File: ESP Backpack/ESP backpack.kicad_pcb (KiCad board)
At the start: 2 copper layers, 100 x 100 mm, 33 parts, among them J1 HLE-120-02-F-DV-BE-K, J2 HLE-120-02-F-DV-BE-K, U1 ESP32-DEVKITC-32D, U2 VCNL4010-GS08

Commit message: edit weird fill issue
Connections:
- J1 pad 30: Net-(J1-Pad30) -> GND
- J1 pad 34: Net-(J1-Pad34) -> GND
- J1 pad 38: Net-(J1-Pad38) -> GND
- J2 pad 29: Net-(J2-Pad29) -> +5V
- J2 pad 30: Net-(J2-Pad30) -> GND
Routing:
- net Net-(J1-Pad34): track 1.41 -> 0.00 mm
- net GND: track 28.5 -> 29.9 mm

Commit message: reorg to more standard file tree
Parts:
- D1: footprint LED_SK6812 -> _ESP-Backpack-Custom-Libraries:LED_SK6812
- J1, J2: footprint Custom Libraries:SAMTEC_HLE-120-02-F-DV-BE-K -> _ESP-Backpack-Custom-Libraries:SAMTEC_HLE-120-02-F-DV-BE-K
- S1, S2: footprint 452403012014 -> _ESP-Backpack-Custom-Libraries:452403012014
- U1: footprint Custom Libraries:MODULE_ESP32-DEVKITC-32D -> _ESP-Backpack-Custom-Libraries:MODULE_ESP32-DEVKITC-32D
- U2: footprint Custom Libraries:XDCR_VCNL4010-GS08 -> _ESP-Backpack-Custom-Libraries:XDCR_VCNL4010-GS08
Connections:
- J1 pad 30: GND -> Net-(J1-Pad30)
- J1 pad 34: GND -> Net-(J1-Pad34)
- J1 pad 38: GND -> Net-(J1-Pad38)
- J2 pad 29: +5V -> Net-(J2-Pad29)
- J2 pad 30: GND -> Net-(J2-Pad30)
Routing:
- net Net-(J1-Pad34): track 0.00 -> 1.41 mm
- net GND: track 29.9 -> 28.5 mm

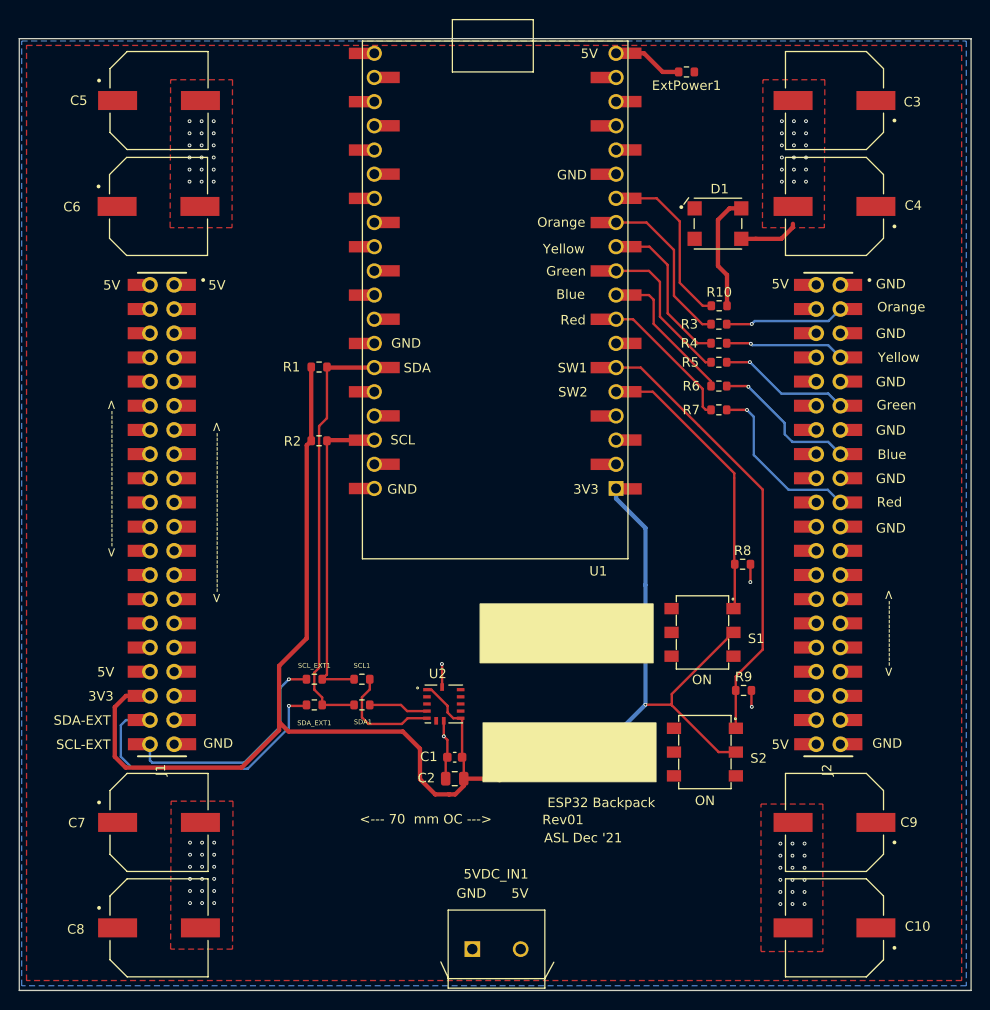
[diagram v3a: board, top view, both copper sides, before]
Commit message: fixes #17, #18, #15 and adds RTC
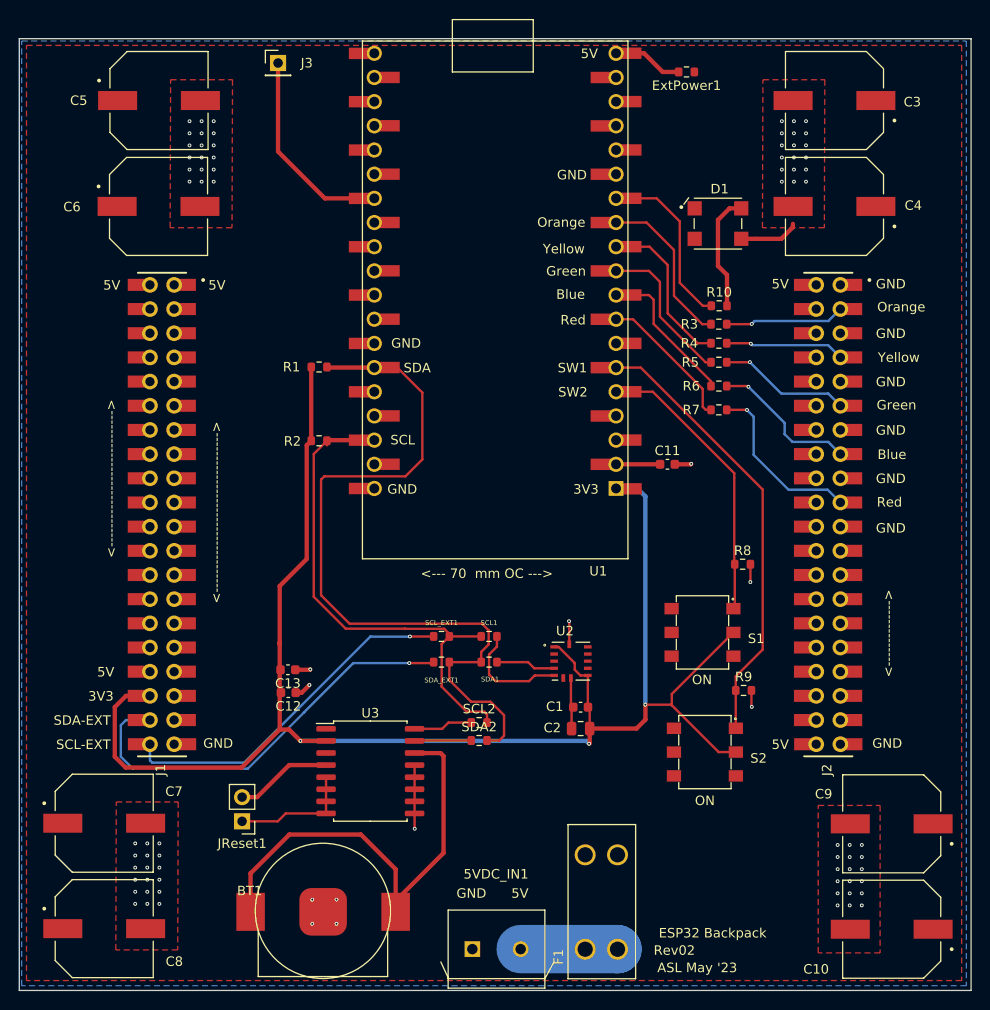
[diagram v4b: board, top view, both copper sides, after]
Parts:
- added BT1: Battery_Cell, _ESP-Backpack-Custom-Libraries:Keystone_2894, F.Cu at (24.3, 91.7)
- added C11: 10uF, Capacitor_SMD:C_0603_1608Metric, F.Cu at (68.1, 44.7)
- added C12: 10uF, Capacitor_SMD:C_0603_1608Metric, F.Cu at (28.3, 68.7)
- added C13: 0.1uF, Capacitor_SMD:C_0603_1608Metric, F.Cu at (28.2, 66.3)
- added F1: Fuse, _ESP-Backpack-Custom-Libraries:Keystone-3658, F.Cu at (59.5, 95.7)
- added J3: Conn_01x01, Connector_PinHeader_2.54mm:PinHeader_1x01_P2.54mm_Vertical, F.Cu at (27.2, 2.56)
- added JReset1: Conn_01x02, Connector_PinHeader_2.54mm:PinHeader_1x02_P2.54mm_Vertical, F.Cu at (23.4, 82.2)
- added SCL2: 0ohm, Resistor_SMD:R_0603_1608Metric, F.Cu at (48.3, 71.9)
- added SDA2: 0ohm, Resistor_SMD:R_0603_1608Metric, F.Cu at (48.3, 73.7)
- added U3: DS3231SN#, Package_SO:SOIC-16W_7.5x10.3mm_P1.27mm, F.Cu at (36.9, 77.0)
- moved C1 14.2 mm to (59.0, 70.2)
- moved C2 14.2 mm to (59.0, 72.5)
- moved SDA1 14.1 mm to (49.4, 65.5)
- moved SDA_EXT1 14.1 mm to (44.4, 65.5)
- moved SCL1 14.1 mm to (49.4, 62.8)
- moved SCL_EXT1 14.1 mm to (44.4, 62.8)
- moved U2 14.1 mm to (58.0, 65.4)
- moved C10 6.01 mm to (91.7, 93.6)
- moved C9 6.01 mm to (91.7, 82.5)
- moved C7 5.76 mm to (8.92, 82.4)
- moved C8 5.76 mm to (8.92, 93.5)
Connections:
- 5VDC_IN1 pad 2: +5V -> Net-(5VDC_IN1-Pad2)
- J2 pad 29: Net-(J2-Pad29) -> +5V
- J2 pad 30: Net-(J2-Pad30) -> GND
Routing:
- net Net-(BT1-Pad1): track 0.00 -> 48.6 mm
- net /SDA: track 44.7 -> 79.7 mm
- net GND: track 28.5 -> 52.5 mm, vias 76 -> 83
- net Net-(J3-Pad1): track 0.00 -> 21.5 mm
- net /SCL: track 32.0 -> 52.8 mm
- net Net-(J1-Pad37): track 30.7 -> 44.6 mm
- net Net-(J1-Pad39): track 24.3 -> 37.1 mm
- net Net-(JReset1-Pad2): track 0.00 -> 10.2 mm
- net Net-(5VDC_IN1-Pad2): track 0.00 -> 10.2 mm
- net Net-(SCL2-Pad1): track 0.00 -> 6.23 mm
- net Net-(SDA2-Pad1): track 0.00 -> 5.98 mm
- net Net-(C11-Pad1): track 0.00 -> 4.63 mm
- net +3V3: track 172.9 -> 170.3 mm, vias 2 -> 3
- net Net-(J1-Pad34): track 1.41 -> 0.00 mm
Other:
- board text added: "ASL May '23"
- board text added: "Rev02"
- board text removed: "ASL Dec '21"
- board text removed: "Rev01"

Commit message: add outputs
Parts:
- moved R5 0.63 mm to (73.5, 34.6)
- moved R4 0.44 mm to (73.5, 32.4)
- moved R6 0.31 mm to (73.5, 36.8)
- moved R3 0.25 mm to (73.5, 30.3)
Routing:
- net Net-(BT1-Pad1): track 48.6 -> 21.6 mm
- net /BlueLine: track 17.0 -> 15.8 mm
- net Net-(R6-Pad1): track 15.7 -> 16.4 mm
